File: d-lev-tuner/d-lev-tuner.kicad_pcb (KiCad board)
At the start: 4 copper layers, 71.1 x 68.4 mm, 45 parts, among them J1 S6B-PH-SM4-TB, U1 STP08CP05, U2 STP08CP05, U3 AP2112K-3.3, U4 STP08CP05

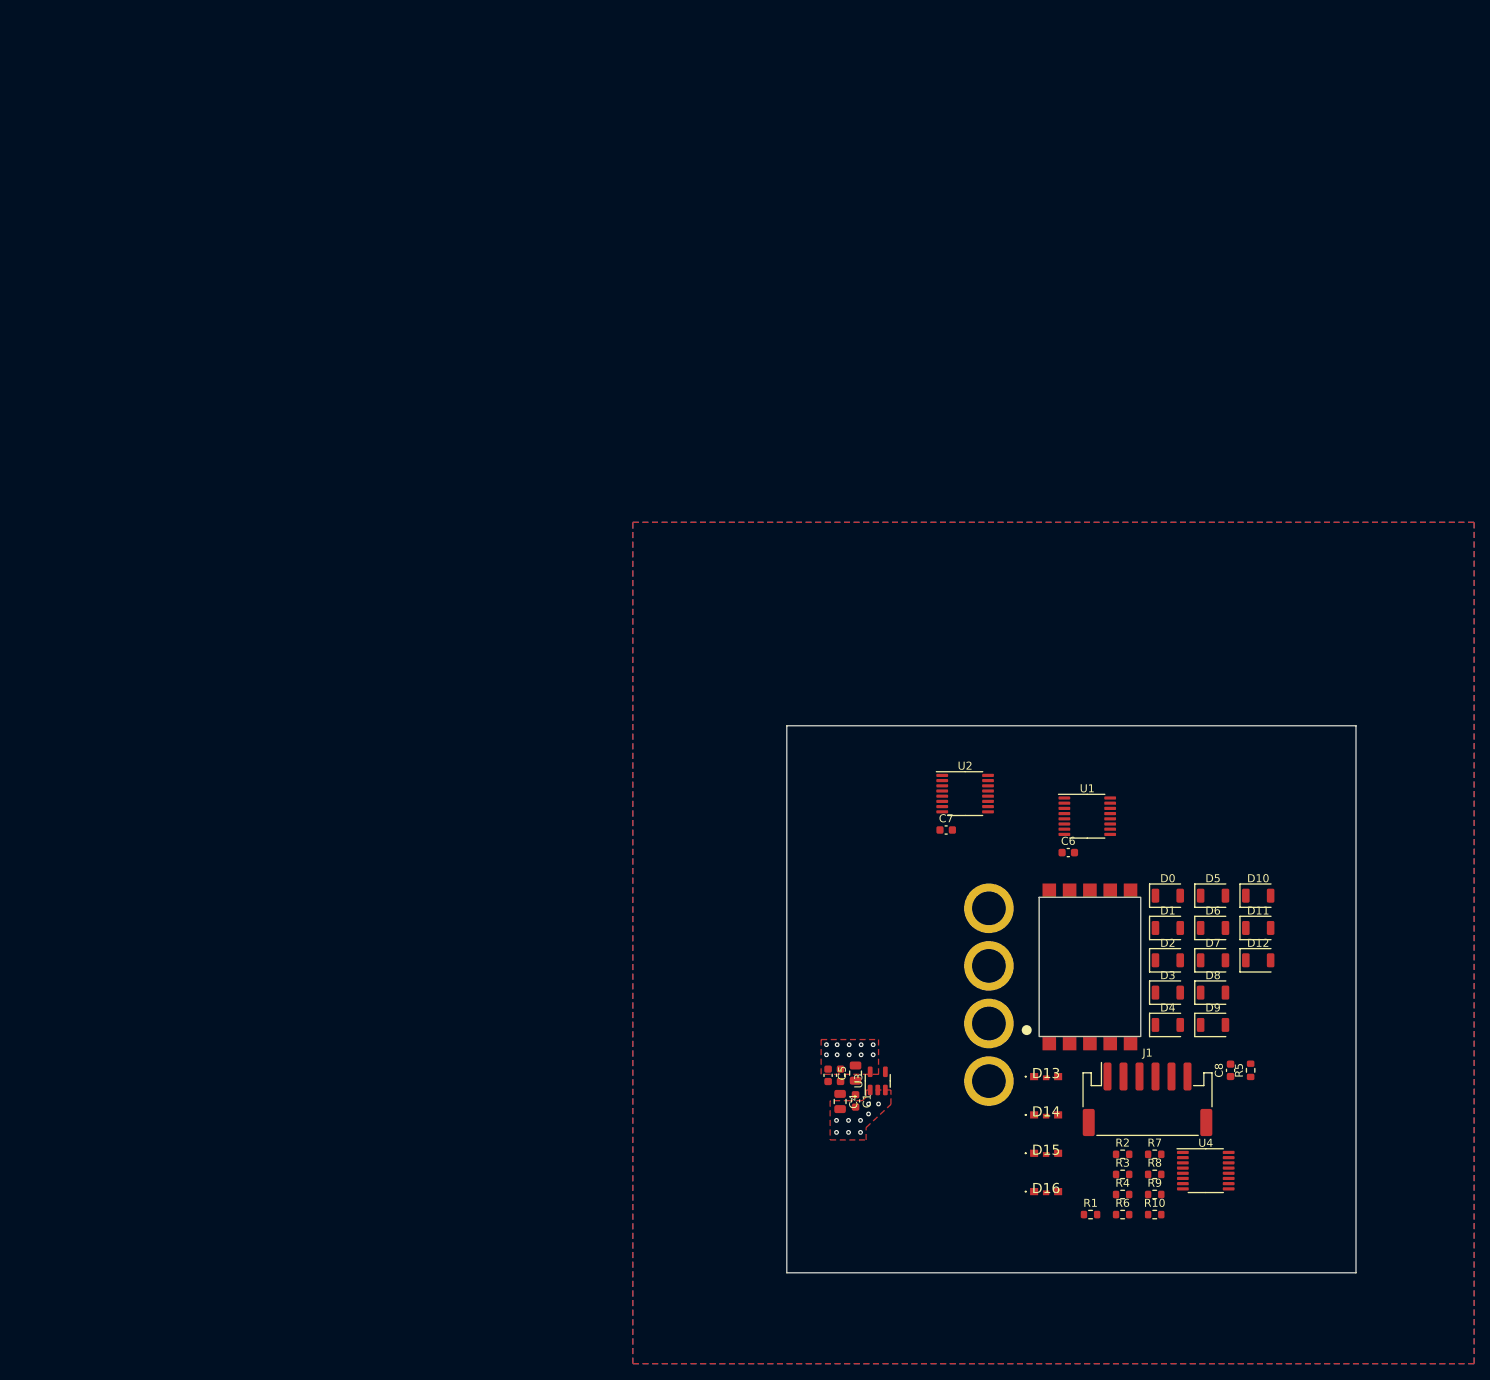
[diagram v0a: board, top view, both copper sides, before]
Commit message: finished routing tuner
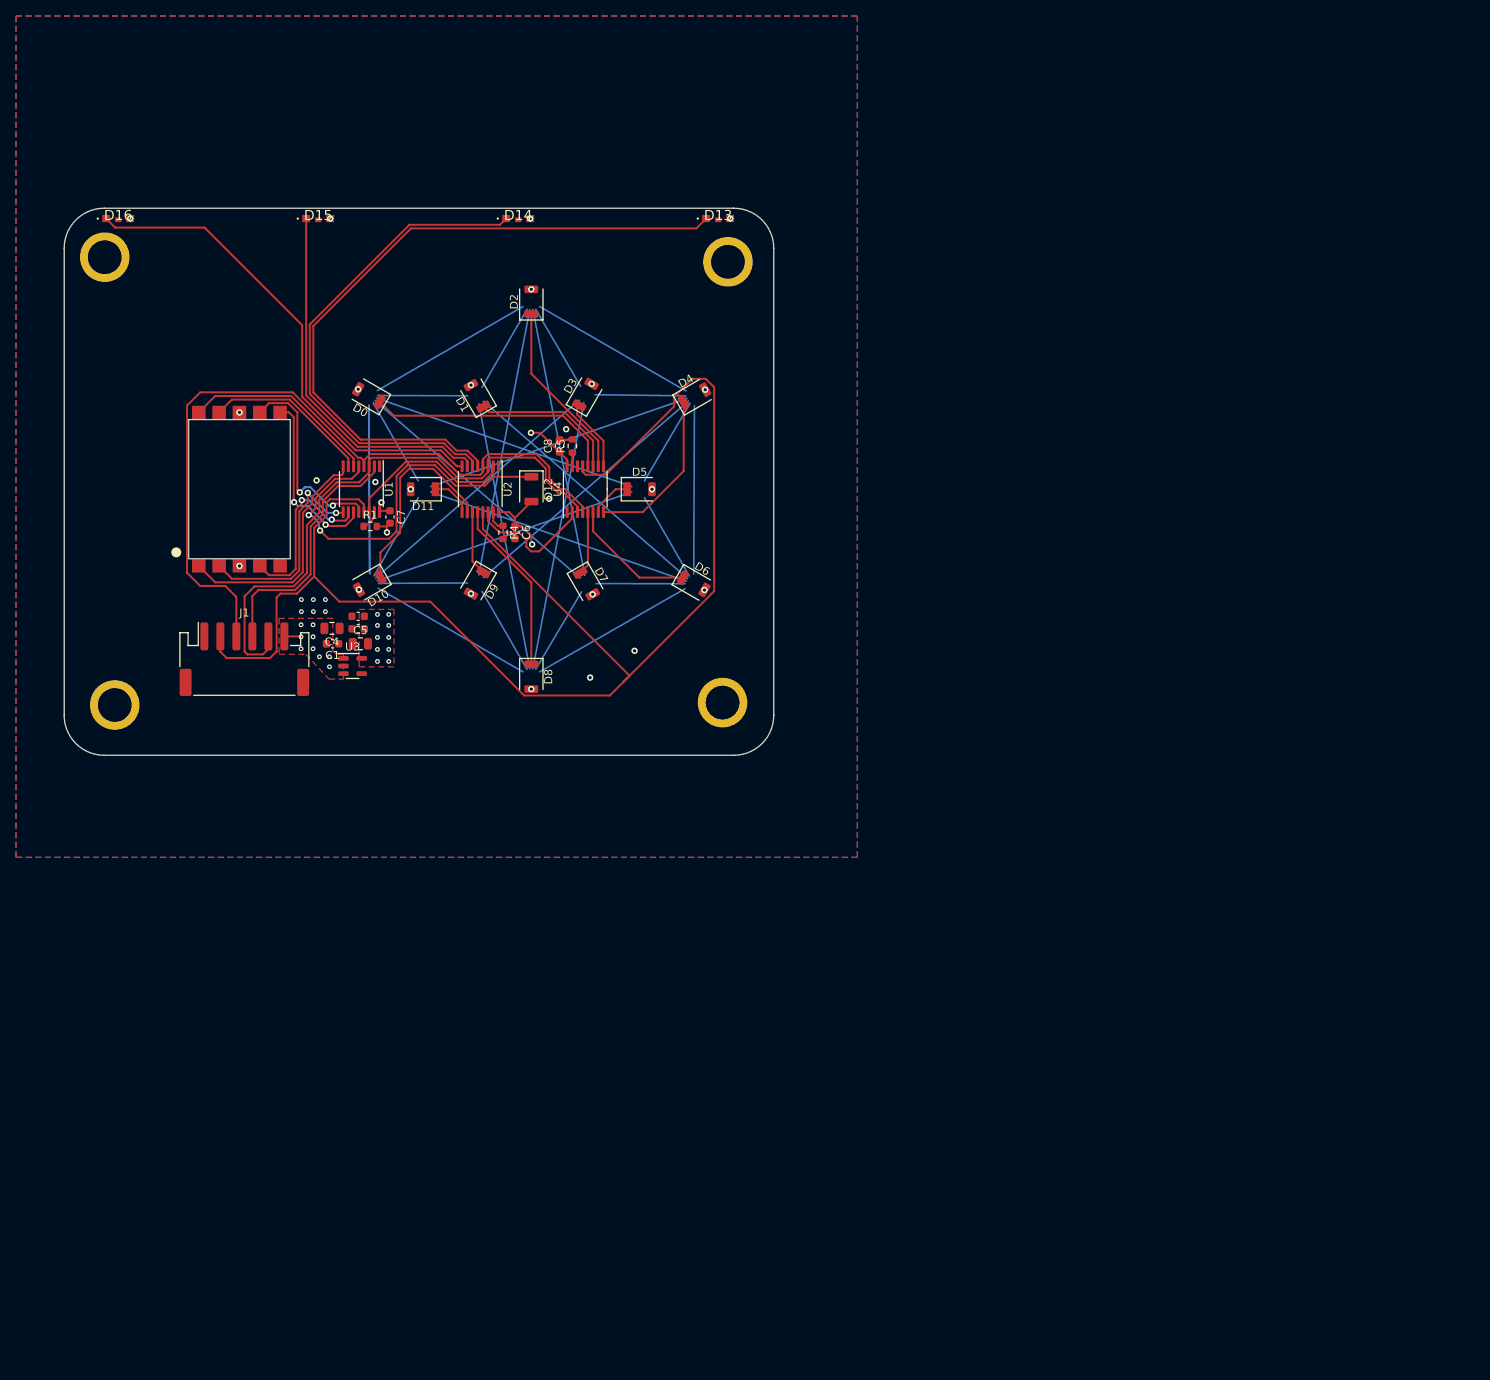
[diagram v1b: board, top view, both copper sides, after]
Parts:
- removed R10, R2, R3, R6, R7, R8, R9: R_Small_US, Resistor_SMD:R_0603_1608Metric
- moved D16 168.1 mm to (48.5, 32.6)
- moved D15 148.1 mm to (73.5, 32.6)
- moved H3 146.3 mm to (46.8, 37.4)
- moved D14 130.0 mm to (98.5, 32.6)
- moved J1 125.6 mm to (64.3, 87.7)
- moved R1 124.5 mm to (80.0, 71.0)
- moved AFF1 121.9 mm to (63.7, 66.4)
- moved H4 119.0 mm to (48.1, 93.4)
- moved D11 117.9 mm to (86.6, 66.4), turned to 180 degrees
- moved D0 117.8 mm to (79.8, 54.7), turned to 150 degrees
- moved D10 117.7 mm to (79.9, 78.2), turned to -150 degrees
- moved R5 115.2 mm to (105.3, 61.0)
- moved U4 115.2 mm to (106.9, 66.4), turned to 90 degrees
- moved D13 114.8 mm to (123.5, 32.6)
- moved C8 114.6 mm to (103.7, 61.0)
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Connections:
- AFF1 pad 1: Net-(AFF1-e) -> E
- AFF1 pad 10: Net-(AFF1-g) -> G
- AFF1 pad 2: Net-(AFF1-d) -> D
- AFF1 pad 4: Net-(AFF1-c) -> C
- AFF1 pad 6: Net-(AFF1-b) -> B
- AFF1 pad 7: Net-(AFF1-a) -> A
- AFF1 pad 9: Net-(AFF1-f) -> F
- J1 pad 1: +5V -> GND
- J1 pad 2: CLK -> OE
- J1 pad 3: SDI -> LE
- J1 pad 4: LE -> SDI
- J1 pad 5: OE -> CLK
- J1 pad 6: GND -> +5V
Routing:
- net OE: track 0.00 -> 177.7 mm
- net LE: track 0.00 -> 96.1 mm
- net LED13: track 0.00 -> 87.7 mm
- net CLK: track 0.00 -> 73.2 mm
- net LED14: track 0.00 -> 63.2 mm
- net LED16: track 0.00 -> 62.6 mm
- net LED12: track 0.00 -> 48.8 mm, vias 0 -> 2
- net LED15: track 0.00 -> 46.3 mm
- net SDI: track 0.00 -> 31.9 mm
- net LED0: track 0.00 -> 31.3 mm
- net E: track 0.00 -> 30.3 mm
- net D: track 0.00 -> 26.8 mm, vias 0 -> 2
- net LED10: track 0.00 -> 25.9 mm
- net A: track 0.00 -> 25.3 mm, vias 0 -> 2
- net G: track 0.00 -> 24.4 mm
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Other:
- board size 71.1 x 68.4 mm -> 88.7 x 68.4 mm

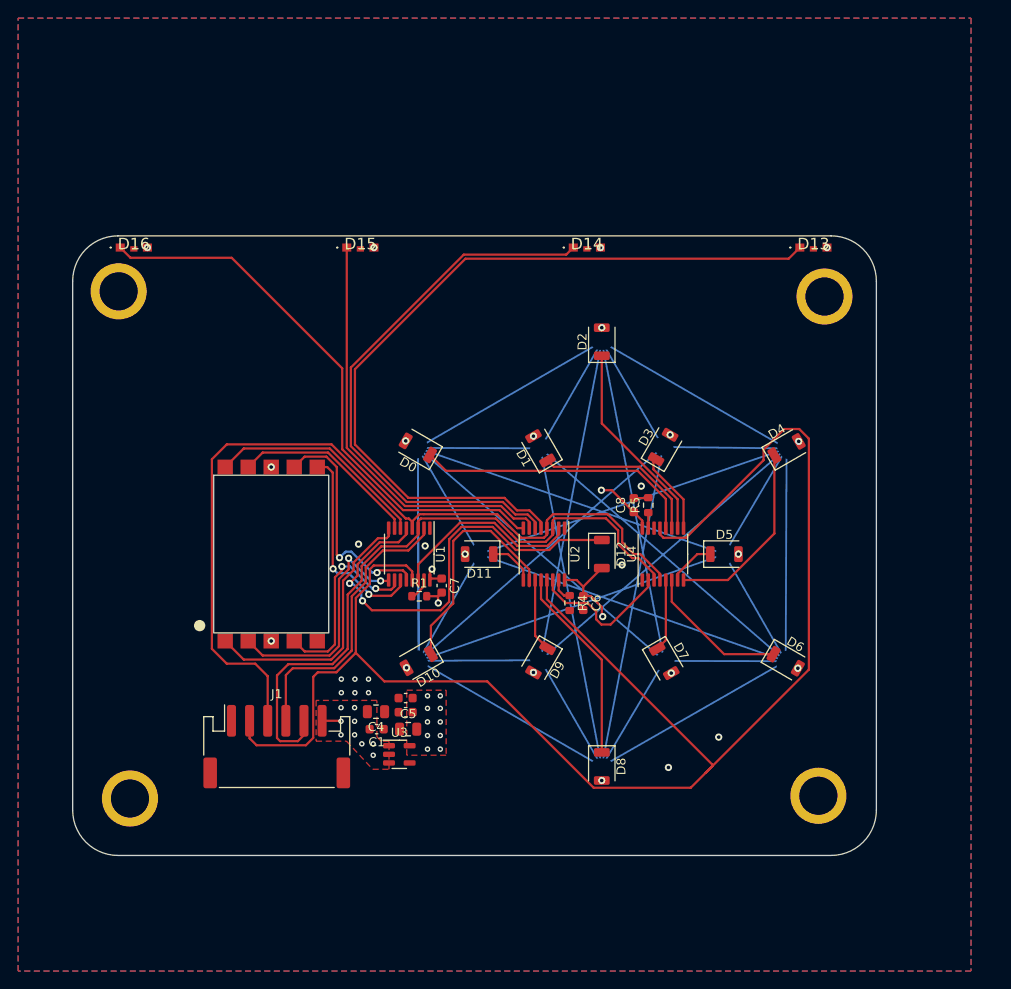
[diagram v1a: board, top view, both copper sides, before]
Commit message: tuner: fix led footprints, reroute, place vias artistically
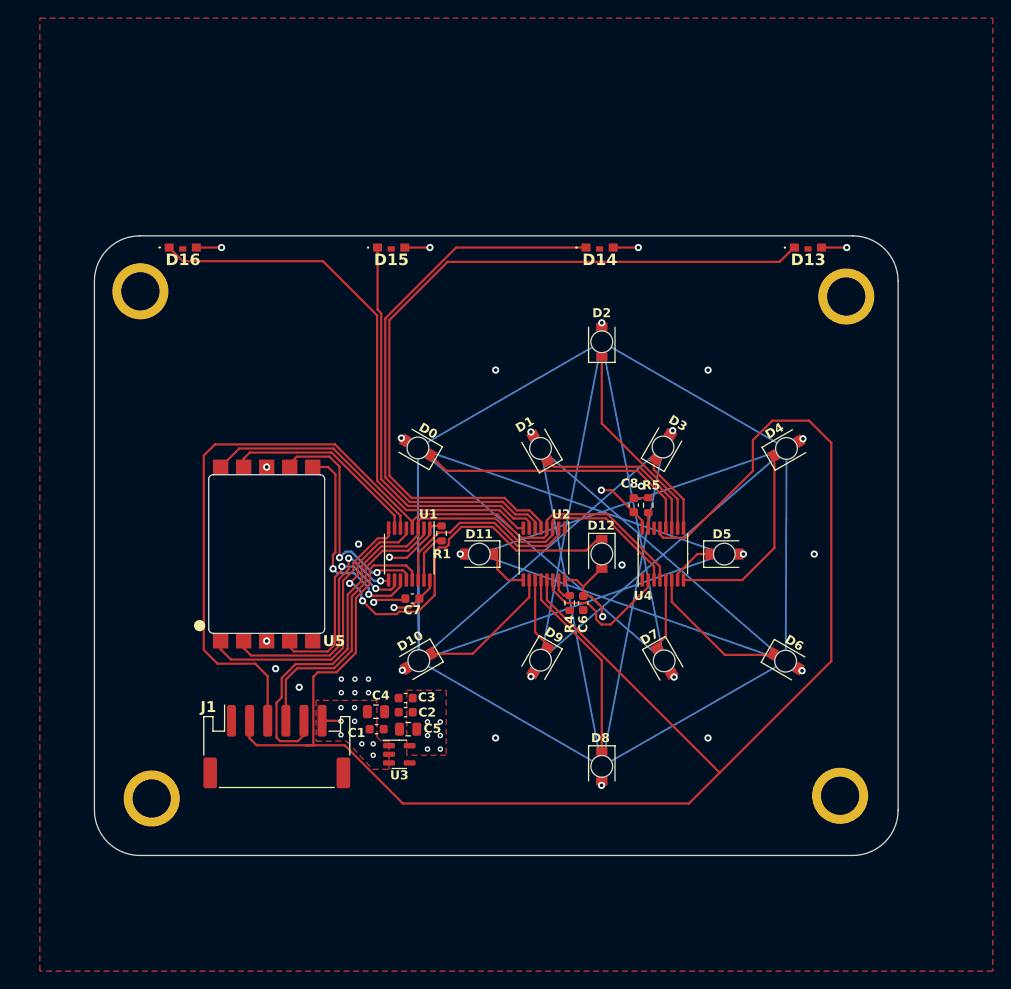
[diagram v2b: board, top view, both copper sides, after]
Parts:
- removed AFF1: DSM7TA56, d-lev:DSM7TA56
- added U5: DSM7TA56, d-lev:DSM7TA56, F.Cu at (63.2, 66.4)
- moved R1 7.35 mm to (82.5, 64.1), turned to 90 degrees
- moved D16 5.40 mm to (53.9, 32.6)
- moved C7 3.54 mm to (79.2, 71.3), turned to 180 degrees
- moved D15 3.40 mm to (76.9, 32.6)
- moved H1 2.40 mm to (126.5, 93.1)
- moved H2 2.40 mm to (127.1, 38.0)
- moved H3 2.40 mm to (49.2, 37.4)
- moved H4 2.40 mm to (50.5, 93.4)
- moved D14 1.40 mm to (99.9, 32.6)
- moved D13 0.60 mm to (122.9, 32.6)
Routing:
- net +3V3: track 19.3 -> 33.5 mm, vias 31 -> 27
- net LED10: track 25.9 -> 14.7 mm
- net OE: track 177.7 -> 187.1 mm
- net GND: track 4.20 -> 12.9 mm, vias 13 -> 18
- net LED13: track 87.7 -> 84.7 mm
- net Net-(U1-R-EXT): track 2.49 -> 5.46 mm
- net LE: track 96.1 -> 97.8 mm
- net LED15: track 46.3 -> 44.7 mm
- net F: track 20.9 -> 22.1 mm
- net E: track 30.3 -> 31.3 mm
- net LED14: track 63.2 -> 62.2 mm
- net D: track 26.8 -> 27.7 mm
- net A: track 25.3 -> 26.2 mm
- net C: track 21.9 -> 22.8 mm
- net LED7: track 7.98 -> 7.13 mm
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- removed copper zone on B.Cu, net GND
